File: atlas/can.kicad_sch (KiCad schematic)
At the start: 5 parts, among them U1801 MCP2562-E-SN

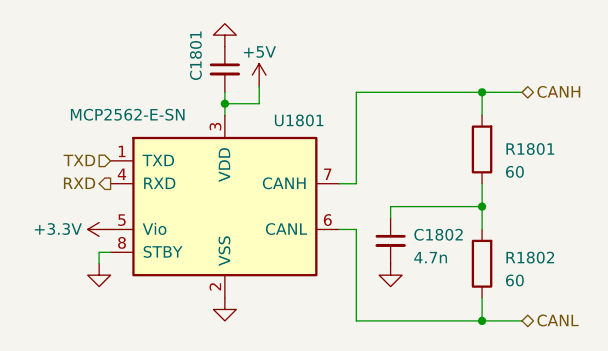
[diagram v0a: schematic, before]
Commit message: footprints & lcsc
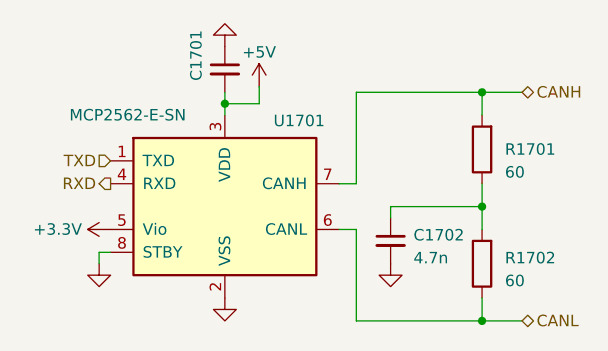
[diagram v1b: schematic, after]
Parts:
- C1702: renamed from C1802; LCSC (none) -> C53987
- renumbered C1801 to C1701, R1801 to R1701, R1802 to R1702, U1801 to U1701
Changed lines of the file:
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@@
   (symbol (lib_id "Device:R") (at 66.675 31.75 180)
     (in_bom yes) (on_board yes)
-    (property "Reference" "R1801" (id 0) (at 69.215 31.7499 0)
+    (property "Reference" "R1701" (id 0) (at 69.215 31.7499 0)
       (effects (font (size 1.27 1.27)) (justify right))
     )
@@
   (symbol (lib_id "Device:R") (at 66.675 44.45 180)
     (in_bom yes) (on_board yes) (fields_autoplaced)
-    (property "Reference" "R1802" (id 0) (at 69.215 43.8149 0)
+    (property "Reference" "R1702" (id 0) (at 69.215 43.8149 0)
       (effects (font (size 1.27 1.27)) (justify right))
     )
@@
   (symbol (lib_id "Device:C_Small") (at 38.1 22.86 0)
     (in_bom yes) (on_board yes)
-    (property "Reference" "C1801" (id 0) (at 34.925 24.1299 90)
+    (property "Reference" "C1701" (id 0) (at 34.925 24.1299 90)
       (effects (font (size 1.27 1.27)) (justify left))
     )
@@
   (symbol (lib_id "Device:C_Small") (at 56.515 41.91 0)
     (in_bom yes) (on_board yes) (fields_autoplaced)
-    (property "Reference" "C1802" (id 0) (at 59.055 41.2749 0)
+    (property "Reference" "C1702" (id 0) (at 59.055 41.2749 0)
       (effects (font (size 1.27 1.27)) (justify left))
     )
@@
       (effects (font (size 1.27 1.27)) hide)
     )
+    (property "LCSC" "C53987" (id 4) (at 56.515 41.91 0)
+      (effects (font (size 1.27 1.27)) hide)
+    )
     (pin "1")
     (pin "2")
@@
   (symbol (lib_id "Interface_CAN_LIN:MCP2562-E-SN") (at 38.1 38.1 0)
     (in_bom yes) (on_board yes)
-    (property "Reference" "U1801" (id 0) (at 46.355 28.575 0))
+    (property "Reference" "U1701" (id 0) (at 46.355 28.575 0))
     (property "Value" "MCP2562-E-SN" (id 1) (at 27.305 27.94 0))
     (property "Footprint" "Package_SO:SOIC-8_3.9x4.9mm_P1.27mm" (id 2) (at 38.1 50.8 0)
